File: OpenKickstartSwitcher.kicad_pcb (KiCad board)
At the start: 2 copper layers, 28.4 x 76.5 mm, 14 parts, among them J1 Conn_01x03, J2 Conn_01x04, J3 A19, J99 OSHW_LOGO, U1 KS_SOCKET, U2 M27C800, U3 7400

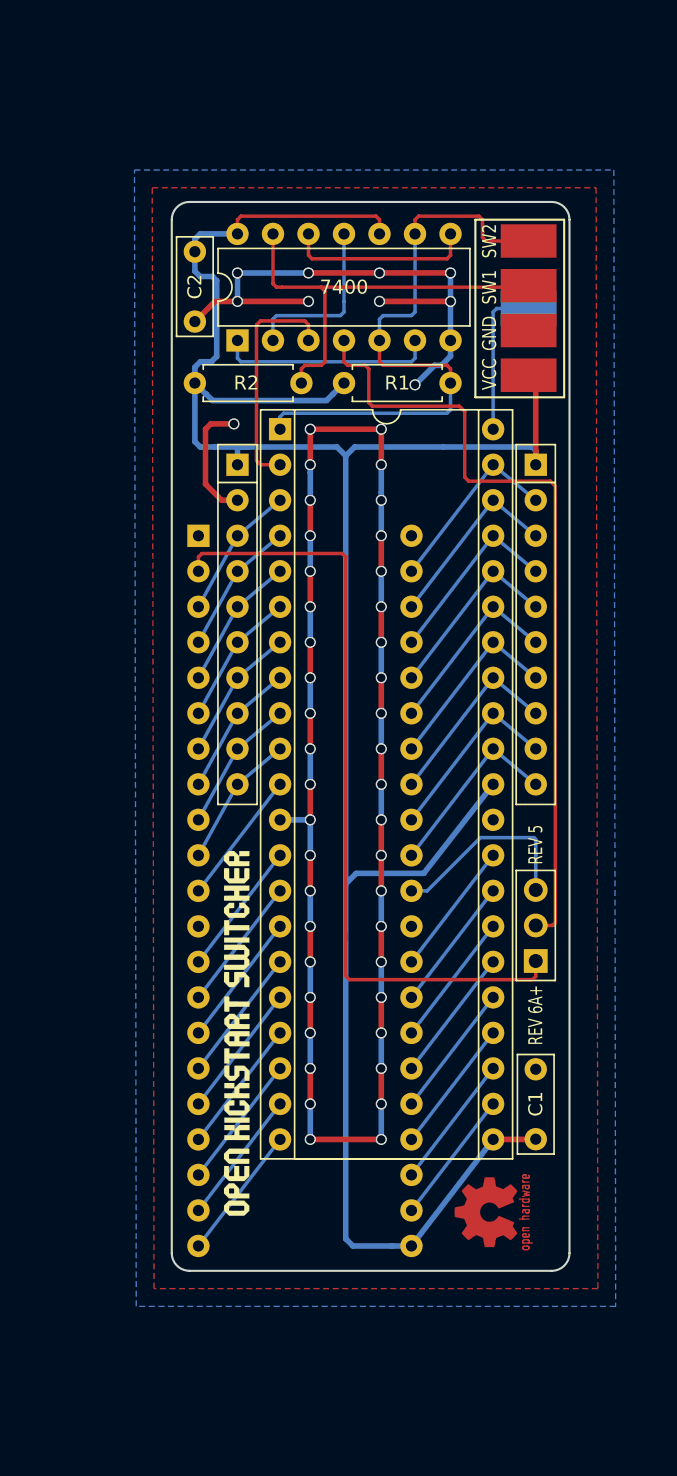
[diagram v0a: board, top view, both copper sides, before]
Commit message: Make logo larger
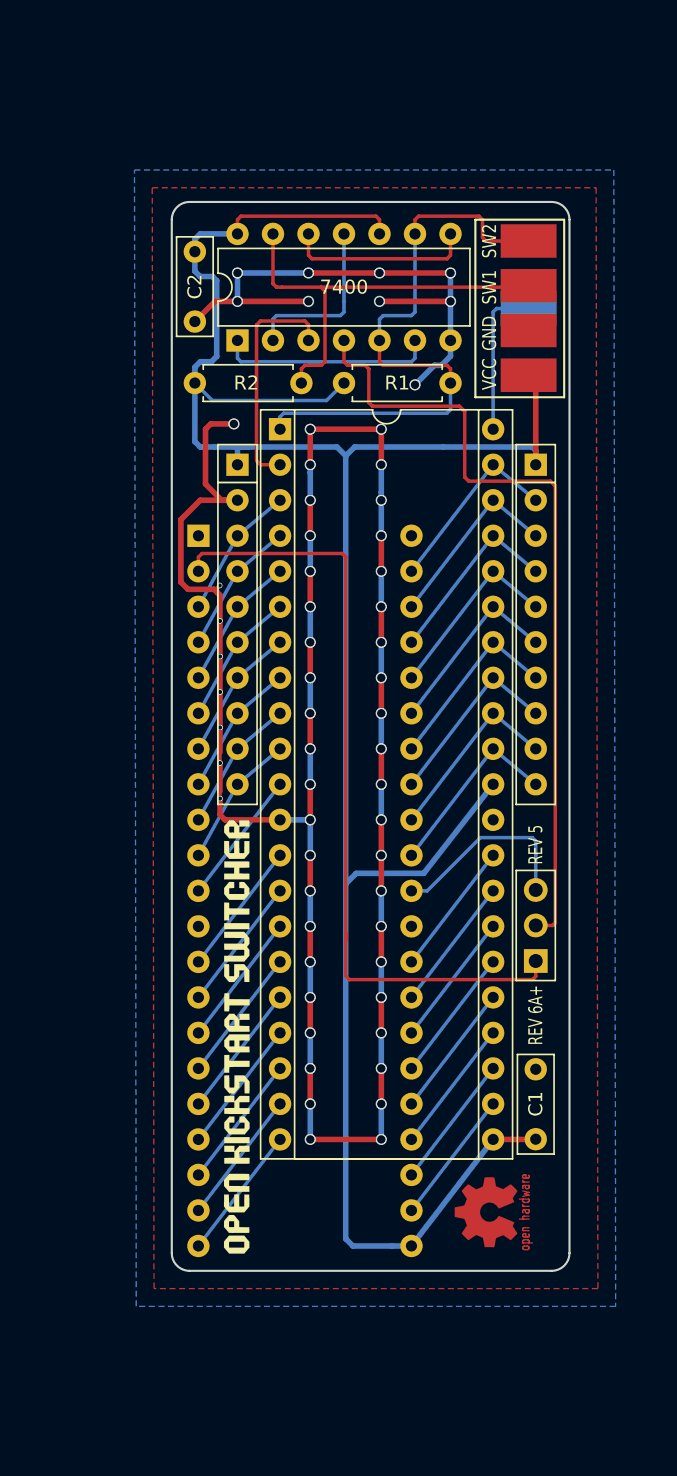
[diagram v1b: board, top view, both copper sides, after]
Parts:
- moved G*** 0.25 mm to (148.3, 148.3)
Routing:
- net GND: track 163.6 -> 196.7 mm, vias 52 -> 59

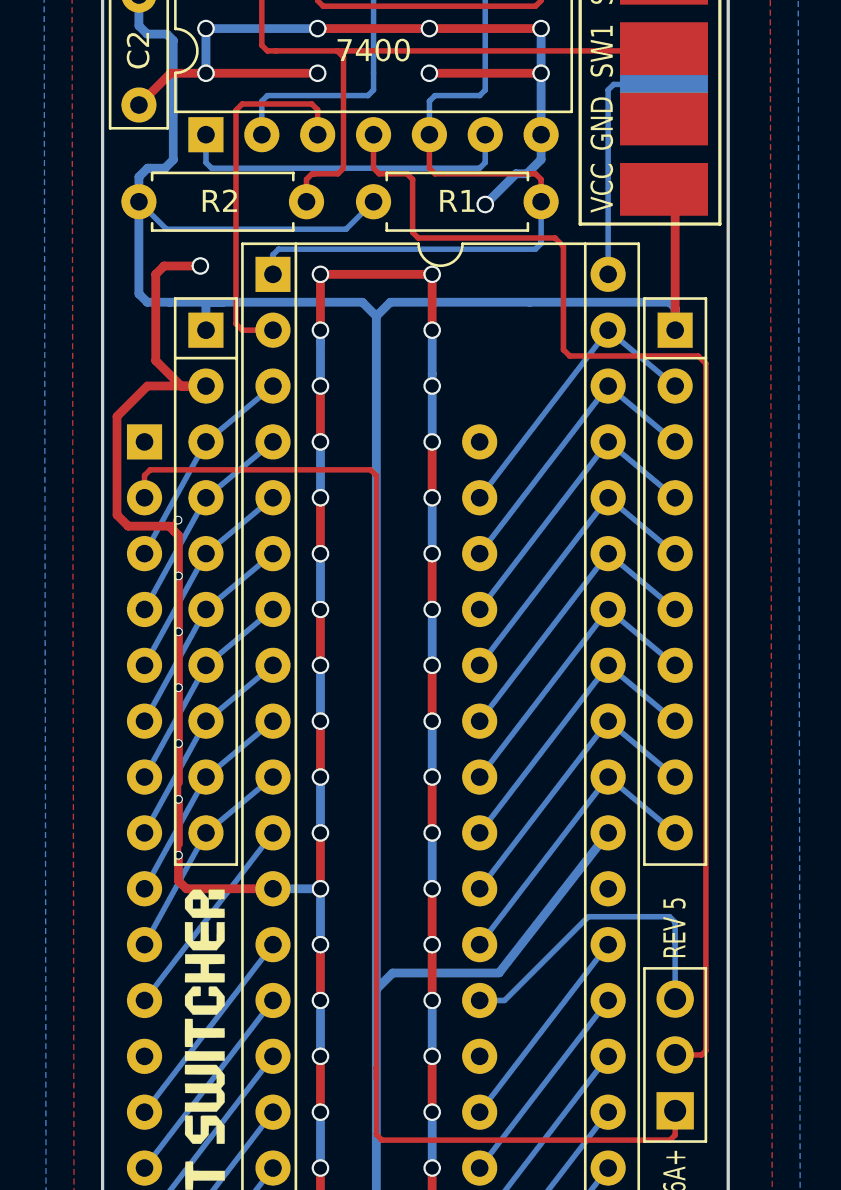
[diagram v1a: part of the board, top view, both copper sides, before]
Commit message: Use smaller footprint for resistors
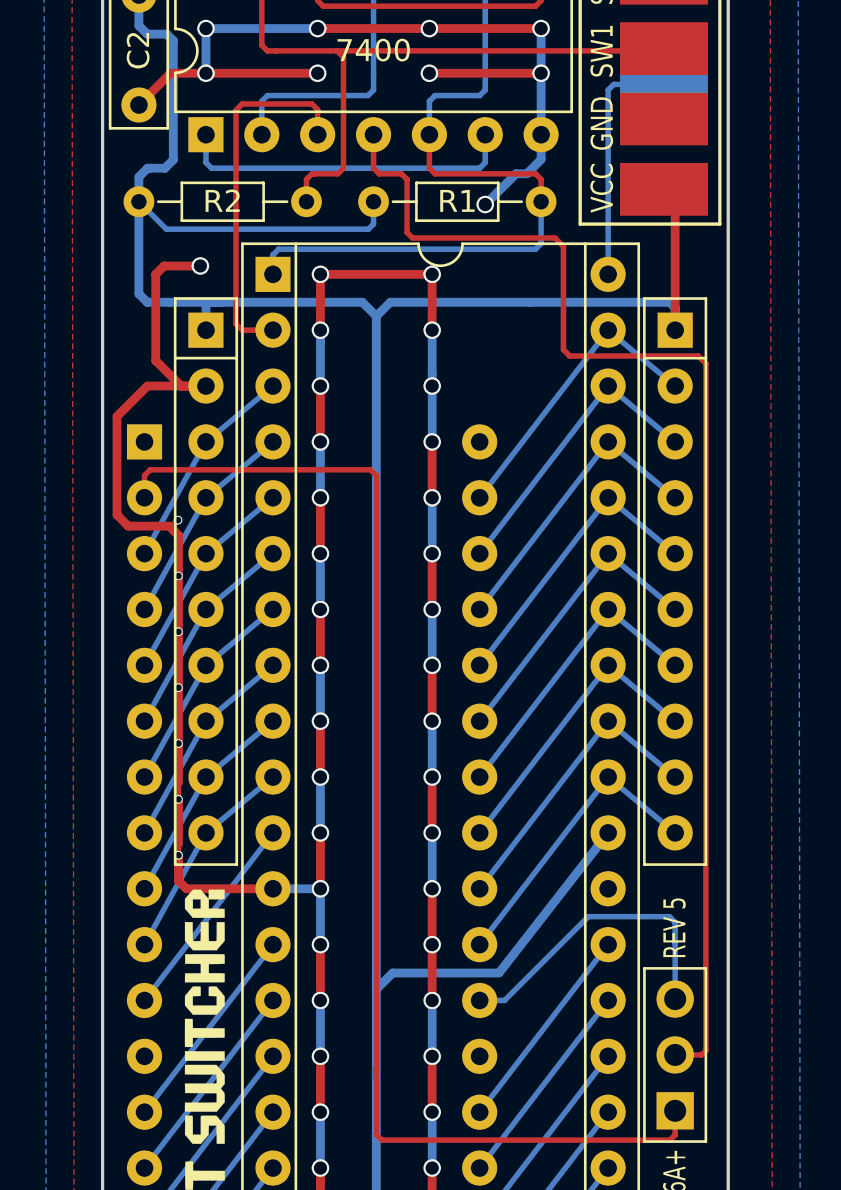
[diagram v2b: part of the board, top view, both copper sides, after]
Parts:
- R1, R2: footprint Resistors_THT:R_Axial_DIN0207_L6.3mm_D2.5mm_P7.62mm_Horizontal -> Resistors_THT:R_Axial_DIN0204_L3.6mm_D1.6mm_P7.62mm_Horizontal
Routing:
- net VCC: track 166.4 -> 167.0 mm

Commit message: Routing improvements
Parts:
- moved R1 7.62 mm to (163.6, 101.6), turned to 180 degrees
- moved C2 5.00 mm to (145.3, 97.2), turned to 90 degrees
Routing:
- net GND: track 196.7 -> 157.1 mm, vias 59 -> 51
- net /sw18: track 43.6 -> 33.5 mm
- net VCC: track 167.0 -> 157.1 mm
- net /a17: track 57.2 -> 60.2 mm
- net Net-(J1-Pad1): track 57.1 -> 54.6 mm

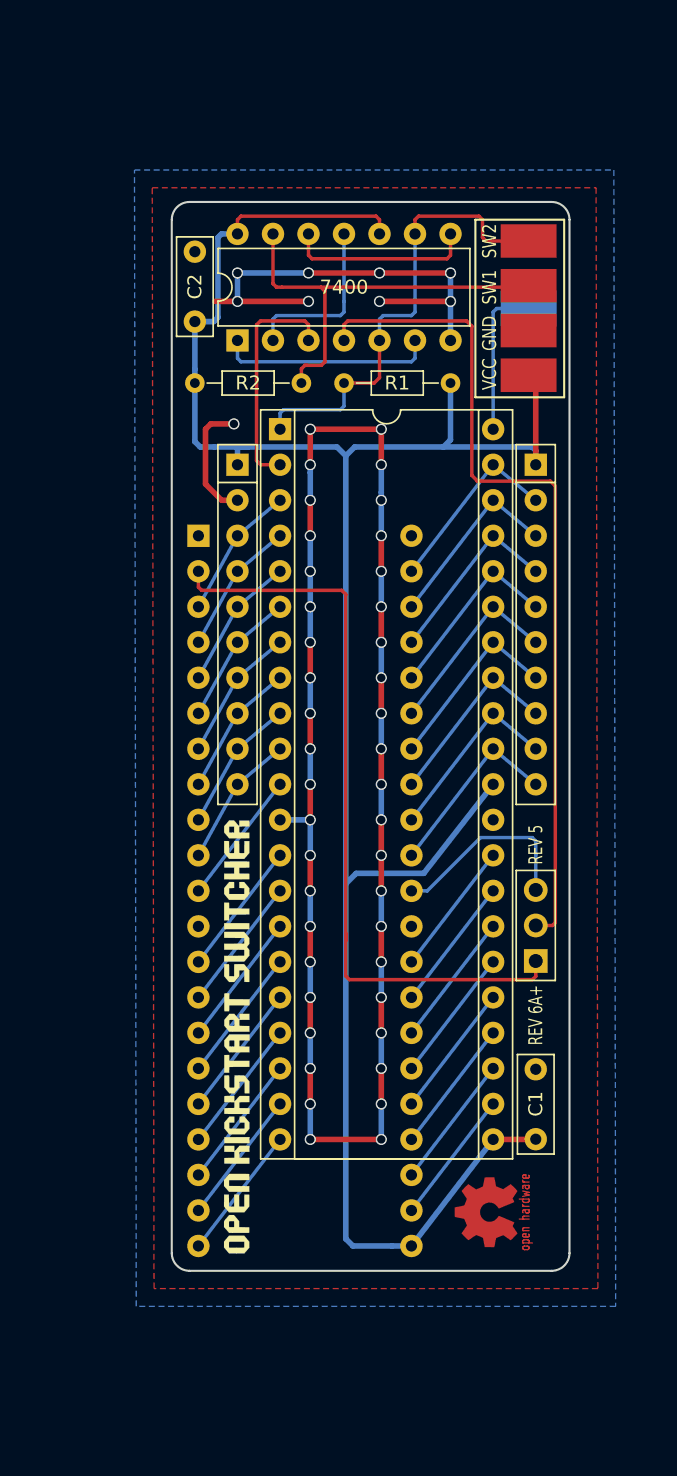
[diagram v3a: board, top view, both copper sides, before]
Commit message: Replace SW3 with a solder jumper
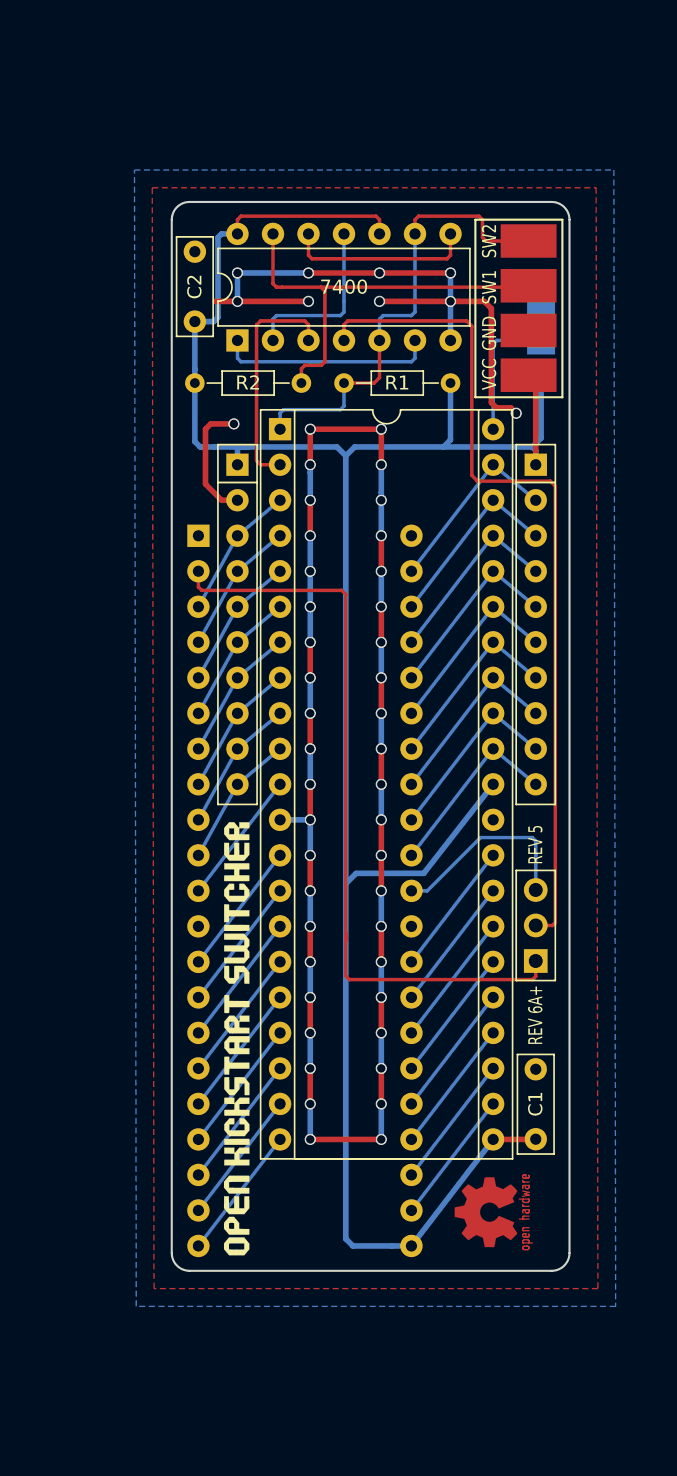
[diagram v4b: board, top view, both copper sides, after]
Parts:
- removed G***: LOGO, logo:logo
- removed J3: A19, OpenKickstartSwitcher:LoosePads-1
- added J4: Conn_01x03, OpenKickstartSwitcher:SolderJumper, B.Cu at (170.1, 98.6)
- added J98: LOGO, logo:logo, F.Cu at (148.3, 148.5)
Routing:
- net GND: track 157.1 -> 168.6 mm, vias 51 -> 52
- net VCC: track 157.1 -> 162.9 mm
- net Net-(J4-Pad2): track 11.0 -> 9.63 mm
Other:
- board text added: "A19"
- board text removed: "SW3"

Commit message: Minor adjustments
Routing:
- net GND: track 168.6 -> 160.3 mm, vias 52 -> 51
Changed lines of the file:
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@@
     (links 87)
     (no_connects 0)
-    (area 130.580001 79.850001 187.300999 178.600937)
+    (area 143.561999 88.570999 172.160001 165.175001)
     (thickness 1.6)
     (drawings 32)
-    (tracks 303)
+    (tracks 299)
     (zones 0)
     (modules 14)
@@
   (title_block
     (title OpenKickstartSwitcher)
-    (date 2018-04-12)
+    (date 2018-04-21)
     (rev V2)
     (company SukkoPera)
@@
     (pad 13 thru_hole oval (at 7.62 2.54 90) (size 1.6 1.6) (drill 0.8) (layers *.Cu *.Mask)
       (net 4 /sw17))
-    (pad 7 thru_hole oval (at 0 15.24 90) (size 1.6 1.6) (drill 0.8) (layers *.Cu *.Mask)
+    (pad 7 thru_hole oval (at 0 15.24 135) (size 1.6 1.6) (drill 0.8) (layers *.Cu *.Mask)
       (net 5 GND))
     (pad 14 thru_hole oval (at 7.62 0 90) (size 1.6 1.6) (drill 0.8) (layers *.Cu *.Mask)
@@
     (effects (font (size 1 1) (thickness 0.15)) (justify mirror))
   )
-  (gr_text A19 (at 167.259 98.552 360) (layer B.SilkS)
+  (gr_text A19 (at 167.259 98.552) (layer B.SilkS)
     (effects (font (size 1 1) (thickness 0.15)) (justify mirror))
   )
@@
   (segment (start 150.876 94.488) (end 151.13 94.742) (width 0.25) (layer F.Cu) (net 4))
   (segment (start 151.13 94.742) (end 151.511 94.742) (width 0.25) (layer F.Cu) (net 4))
+  (segment (start 164.141685 95.758) (end 165.354 95.758) (width 0.4) (layer F.Cu) (net 5))
+  (segment (start 165.354 95.758) (end 165.989 95.758) (width 0.4) (layer F.Cu) (net 5))
   (segment (start 166.878 103.378) (end 167.894 103.378) (width 0.4) (layer F.Cu) (net 5))
   (segment (start 167.894 103.378) (end 168.275 103.759) (width 0.4) (layer F.Cu) (net 5))
@@
   (segment (start 166.497 96.266) (end 166.497 102.997) (width 0.4) (layer F.Cu) (net 5))
   (segment (start 165.989 95.758) (end 166.497 96.266) (width 0.4) (layer F.Cu) (net 5))
-  (segment (start 164.141685 95.758) (end 165.989 95.758) (width 0.4) (layer F.Cu) (net 5))
   (segment (start 163.576 95.758) (end 164.141685 95.758) (width 0.4) (layer F.Cu) (net 5))
-  (segment (start 148.336 109.982) (end 147.20463 109.982) (width 0.4) (layer F.Cu) (net 5))
-  (segment (start 147.20463 109.982) (end 146.05 108.82737) (width 0.4) (layer F.Cu) (net 5))
-  (segment (start 146.05 108.82737) (end 146.05 104.902) (width 0.4) (layer F.Cu) (net 5))
-  (segment (start 146.05 104.902) (end 146.431 104.521) (width 0.4) (layer F.Cu) (net 5))
-  (segment (start 146.431 104.521) (end 148.082 104.521) (width 0.4) (layer F.Cu) (net 5))
-  (segment (start 148.336 95.758) (end 146.732 95.758) (width 0.4) (layer F.Cu) (net 5))
-  (via (at 148.082 104.521) (size 0.8) (drill 0.6) (layers F.Cu B.Cu) (net 5))
-  (segment (start 158.623 153.162) (end 158.623 155.702) (width 0.4) (layer B.Cu) (net 5))
-  (via (at 158.623 155.702) (size 0.8) (drill 0.6) (layers F.Cu B.Cu) (net 5))
-  (segment (start 153.543 153.162) (end 153.543 155.702) (width 0.4) (layer B.Cu) (net 5))
-  (via (at 153.543 155.702) (size 0.8) (drill 0.6) (layers F.Cu B.Cu) (net 5))
-  (segment (start 158.623 140.462) (end 158.623 137.922) (width 0.4) (layer B.Cu) (net 5))
-  (via (at 158.623 137.922) (size 0.8) (drill 0.6) (layers F.Cu B.Cu) (net 5))
-  (segment (start 151.384 132.842) (end 153.543 132.842) (width 0.4) (layer B.Cu) (net 5))
   (segment (start 163.576 95.758) (end 158.496 95.758) (width 0.4) (layer F.Cu) (net 5))
   (via (at 158.496 95.758) (size 0.8) (drill 0.6) (layers F.Cu B.Cu) (net 5))
@@
   (segment (start 163.576 95.758) (end 163.576 93.726) (width 0.4) (layer B.Cu) (net 5))
   (via (at 163.576 95.758) (size 0.8) (drill 0.6) (layers F.Cu B.Cu) (net 5))
-  (segment (start 163.576 98.552) (end 163.576 95.758) (width 0.4) (layer B.Cu) (net 5))
   (segment (start 158.496 93.726) (end 163.576 93.726) (width 0.4) (layer F.Cu) (net 5))
   (via (at 163.576 93.726) (size 0.8) (drill 0.6) (layers F.Cu B.Cu) (net 5))
@@
   (via (at 153.416 93.726) (size 0.8) (drill 0.6) (layers F.Cu B.Cu) (net 5))
   (via (at 148.336 93.726) (size 0.8) (drill 0.6) (layers F.Cu B.Cu) (net 5))
+  (segment (start 165.1 95.758) (end 163.576 95.758) (width 0.4) (layer B.Cu) (net 5))
+  (segment (start 165.1 97.028) (end 165.1 95.758) (width 0.4) (layer B.Cu) (net 5))
+  (segment (start 163.576 98.552) (end 165.1 97.028) (width 0.4) (layer B.Cu) (net 5))
+  (segment (start 158.623 153.162) (end 158.623 155.702) (width 0.4) (layer B.Cu) (net 5))
+  (via (at 158.623 155.702) (size 0.8) (drill 0.6) (layers F.Cu B.Cu) (net 5))
+  (segment (start 153.543 153.162) (end 153.543 155.702) (width 0.4) (layer B.Cu) (net 5))
+  (via (at 153.543 155.702) (size 0.8) (drill 0.6) (layers F.Cu B.Cu) (net 5))
+  (segment (start 158.623 140.462) (end 158.623 137.922) (width 0.4) (layer B.Cu) (net 5))
+  (via (at 158.623 137.922) (size 0.8) (drill 0.6) (layers F.Cu B.Cu) (net 5))
+  (segment (start 151.384 132.842) (end 153.543 132.842) (width 0.4) (layer B.Cu) (net 5))
   (segment (start 153.543 104.902) (end 158.623 104.902) (width 0.4) (layer F.Cu) (net 5))
   (via (at 153.543 104.902) (size 0.8) (drill 0.6) (layers F.Cu B.Cu) (net 5))
@@
   (segment (start 148.336 99.822) (end 148.336 98.552) (width 0.25) (layer B.Cu) (net 44))
   (segment (start 148.336 99.822) (end 148.59 100.076) (width 0.25) (layer B.Cu) (net 44))
-  (segment (start 169.672 140.3985) (end 170.874081 140.3985) (width 0.25) (layer F.Cu) (net 45))
-  (segment (start 170.874081 140.3985) (end 171.069 140.203581) (width 0.25) (layer F.Cu) (net 45))
-  (segment (start 170.720001 108.617001) (end 165.481 108.617001) (width 0.25) (layer F.Cu) (net 45))
-  (segment (start 156.22163 97.155) (end 155.956 97.42063) (width 0.25) (layer F.Cu) (net 45))
-  (segment (start 171.069 140.203581) (end 171.069 108.966) (width 0.25) (layer F.Cu) (net 45))
-  (segment (start 171.069 108.966) (end 170.720001 108.617001) (width 0.25) (layer F.Cu) (net 45))
-  (segment (start 165.481 108.617001) (end 165.481 108.585) (width 0.25) (layer F.Cu) (net 45))
-  (segment (start 165.481 108.585) (end 165.1 108.204) (width 0.25) (layer F.Cu) (net 45))
-  (segment (start 165.1 108.204) (end 165.1 97.536) (width 0.25) (layer F.Cu) (net 45))
-  (segment (start 165.1 97.536) (end 164.719 97.155) (width 0.25) (layer F.Cu) (net 45))
-  (segment (start 164.719 97.155) (end 156.22163 97.155) (width 0.25) (layer F.Cu) (net 45))
-  (segment (start 155.956 97.42063) (end 155.956 98.552) (width 0.25) (layer F.Cu) (net 45))
+  (segment (start 155.956 98.552) (end 155.956 97.42063) (width 0.25) (layer F.Cu) (net 45))
+  (segment (start 155.956 97.42063) (end 156.22163 97.155) (width 0.25) (layer F.Cu) (net 45))
+  (segment (start 156.22163 97.155) (end 164.719 97.155) (width 0.25) (layer F.Cu) (net 45))
+  (segment (start 164.719 97.155) (end 165.1 97.536) (width 0.25) (layer F.Cu) (net 45))
+  (segment (start 165.481 108.585) (end 165.481 108.617001) (width 0.25) (layer F.Cu) (net 45))
+  (segment (start 165.1 97.536) (end 165.1 108.204) (width 0.25) (layer F.Cu) (net 45))
+  (segment (start 165.1 108.204) (end 165.481 108.585) (width 0.25) (layer F.Cu) (net 45))
+  (segment (start 170.720001 108.617001) (end 171.069 108.966) (width 0.25) (layer F.Cu) (net 45))
+  (segment (start 171.069 108.966) (end 171.069 140.203581) (width 0.25) (layer F.Cu) (net 45))
+  (segment (start 165.481 108.617001) (end 170.720001 108.617001) (width 0.25) (layer F.Cu) (net 45))
+  (segment (start 170.874081 140.3985) (end 169.672 140.3985) (width 0.25) (layer F.Cu) (net 45))
+  (segment (start 171.069 140.203581) (end 170.874081 140.3985) (width 0.25) (layer F.Cu) (net 45))
   (segment (start 155.956 96.52) (end 155.956 95.758) (width 0.25) (layer B.Cu) (net 46))
   (segment (start 155.702 96.774) (end 155.956 96.52) (width 0.25) (layer B.Cu) (net 46))
